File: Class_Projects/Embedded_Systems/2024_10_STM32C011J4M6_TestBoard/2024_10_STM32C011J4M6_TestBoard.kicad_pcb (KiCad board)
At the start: 2 copper layers, 25 x 25 mm, 22 parts, among them J2 SWD_Conn, J3 USB_C_Receptacle_USB2.0_14P, U1 STM32C011J4Mx, U2 FT230XS, U3 LD1117S33TR_SOT223

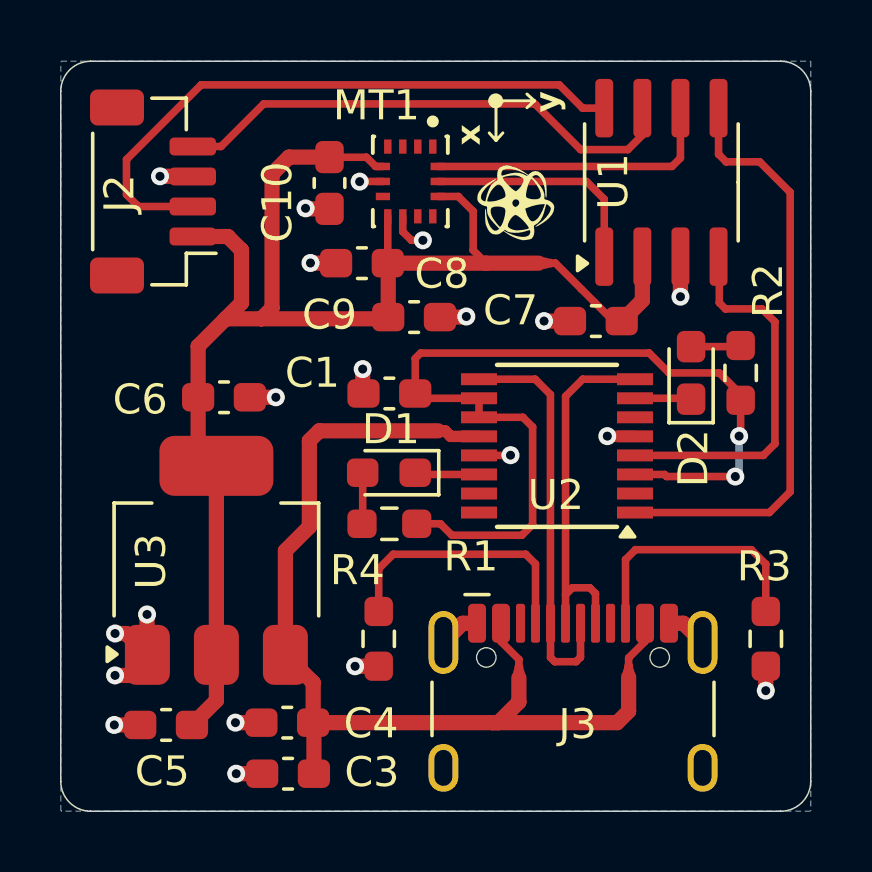
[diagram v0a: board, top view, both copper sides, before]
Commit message: I2C resistor addded to the PCB
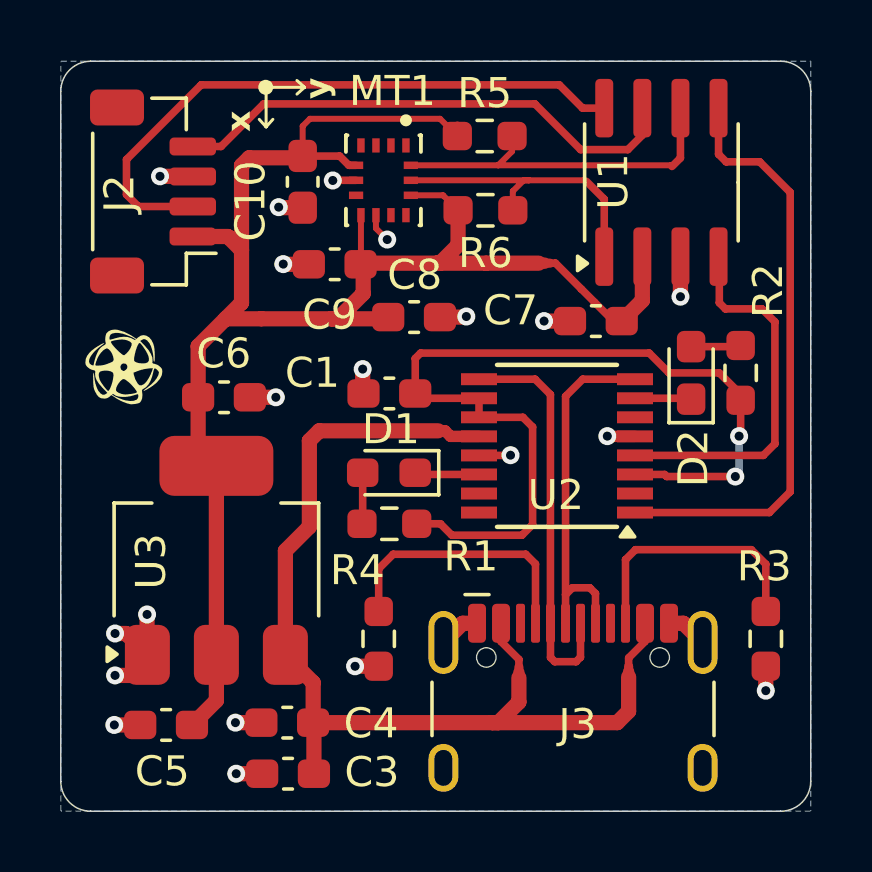
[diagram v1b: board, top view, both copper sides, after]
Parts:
- added R5: 4.7k, Resistor_SMD:R_0603_1608Metric_Pad0.98x0.95mm_HandSolder, F.Cu at (121.1, 68.3)
- added R6: 4.7k, Resistor_SMD:R_0603_1608Metric_Pad0.98x0.95mm_HandSolder, F.Cu at (121.1, 70.7)
- moved G*** 14.2 mm to (109.0, 75.9)
- moved C8 0.91 mm to (116.1, 72.5)
- moved C10 0.90 mm to (115.0, 69.8)
- moved MT1 0.90 mm to (117.7, 69.7)
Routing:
- net +3.3V: track 51.0 -> 58.0 mm
- net /I2C_SCL: track 7.71 -> 9.95 mm
- net /I2C_SDA: track 9.87 -> 11.9 mm
